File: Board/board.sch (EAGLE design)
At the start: 31 parts, among them IC1 MCP2300X/SO, IC2 LM1117, U1 ADS1015

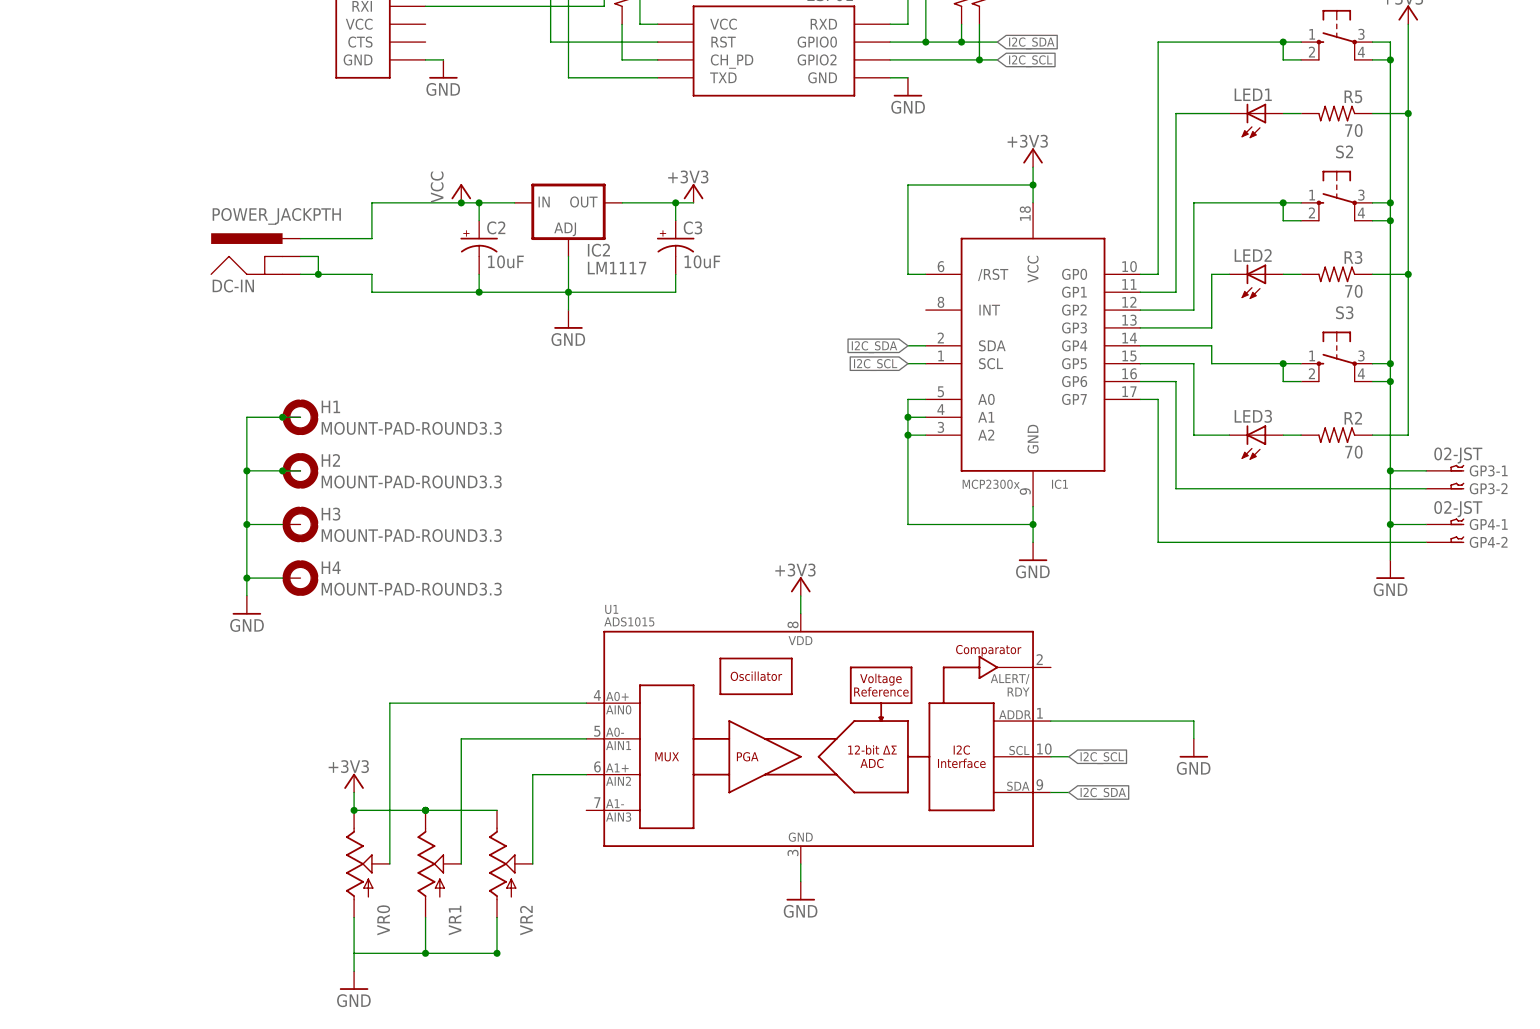
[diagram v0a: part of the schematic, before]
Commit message: Use cheaper ADC and add LEDs on spare GPIO
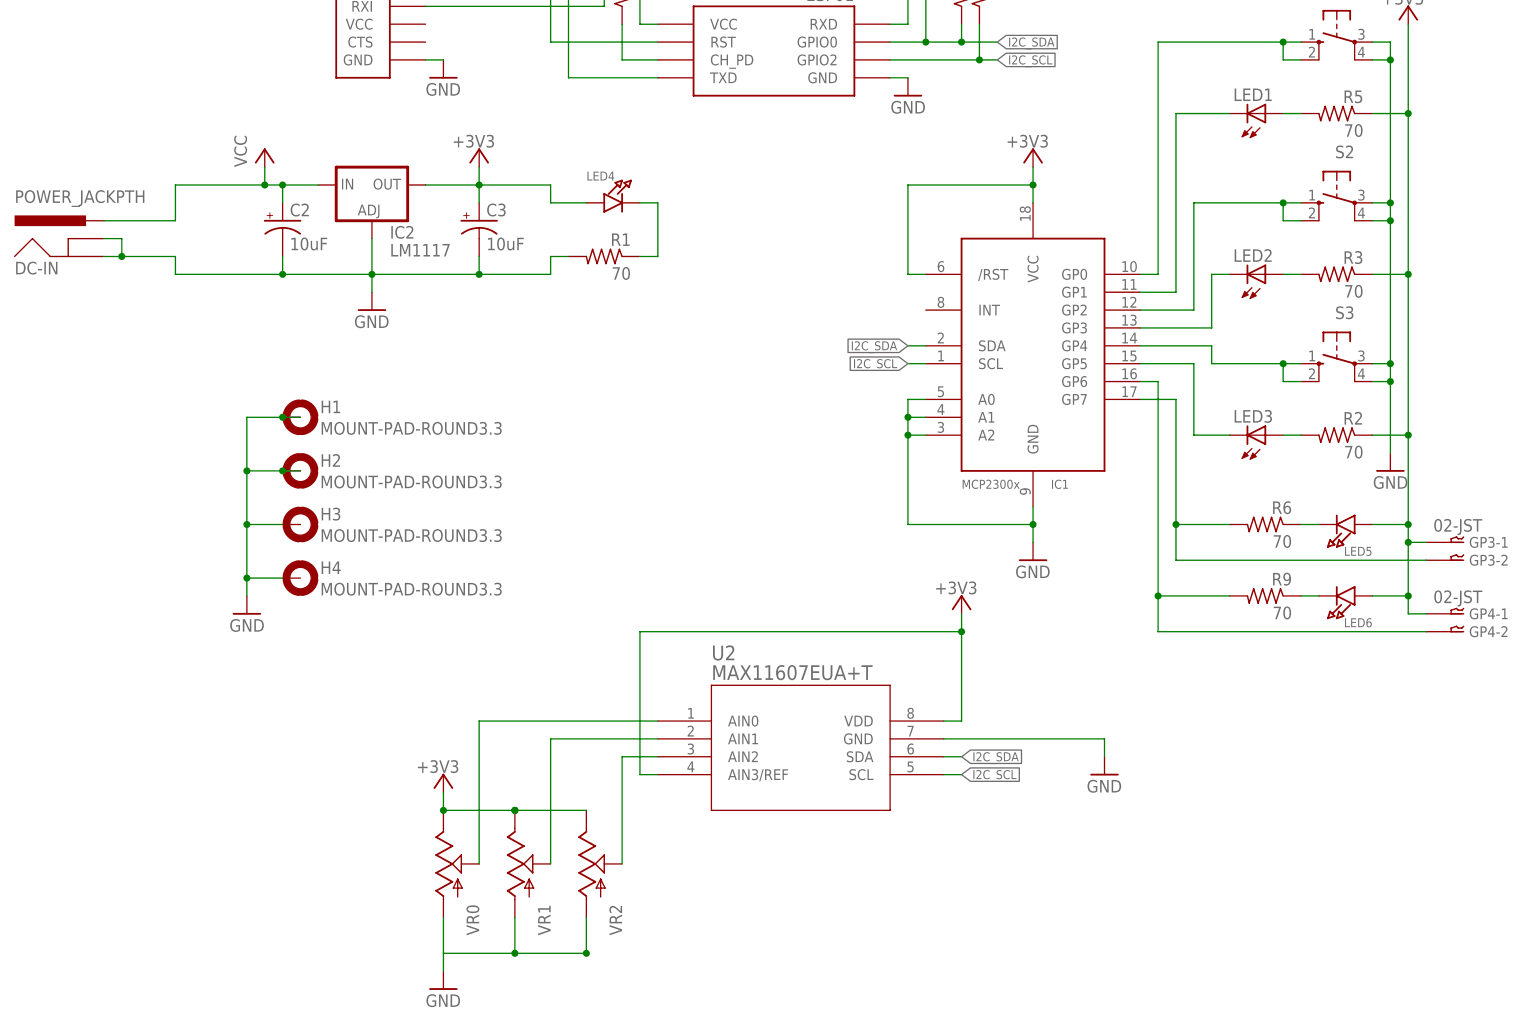
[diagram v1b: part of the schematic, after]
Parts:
- removed U1: ADS1015, SparkFun-AnalogIC:ADS1015
- added LED4, LED5, LED6: (no value), microbuilder:LED0805
- added R1, R6, R9: 70, resistor:R-US_R0603
- added U2: MAX11607EUA+T, MAX11607:MAX11607EUA+T
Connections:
- new net N$11: LED6.C, R9.1
- new net N$7: LED4.C, R1.1
- new net N$9: LED5.C, R6.1
- net +3V3: now also GP3-1.1, GP4-1.1, LED4.A, LED5.A, LED6.A, U2.AIN3/REF, U2.VDD; no longer U1.VDD
- net GND: now also R1.2, U2.GND; no longer GP3-1.1, GP4-1.1, U1.ADDR, U1.VSS
- net GP6: now also IC1.GP7, R6.2; no longer IC1.GP6
- net GP7: now also IC1.GP6, R9.2; no longer IC1.GP7
- net I2C_SCL: now also U2.SCL; no longer U1.SCL
- net I2C_SDA: now also U2.SDA; no longer U1.SDA
- net N$3: now also U2.AIN2; no longer U1.AIN2
- net N$4: now also U2.AIN1; no longer U1.AIN1
- net N$5: now also U2.AIN0; no longer U1.AIN0
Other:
- moved on the sheet: C2, C3, DC-IN, GP3-1, GP3-2, GP4-1, GP4-2, IC2, VR0, VR1, VR2

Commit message: Finish routing PCB
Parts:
- removed D4: (no value), diode:DIODE-DO214AC
- removed DC-IN: POWER_JACKPTH, SparkFun-Connectors:POWER_JACKPTH
- removed ESP-01: ESP01, esp8266modules-pk:ESP01
- removed GP3, GP4: 02-JST, con-jst-xh:02-JST
- removed IC1: MCP2300X/SO, adafruit:MCP2300X/SO
- removed JP2: FTDI_DEVICE, SparkFun-Connectors:FTDI_DEVICE
- removed LED5, LED6: (no value), microbuilder:LED0805
- removed U2: MAX11607EUA+T, MAX11607:MAX11607EUA+T
- added C1: 47pF, rcl:C-USC0603
- added C5: 10nF, rcl:C-USC0603
- added D1, D2, D3: (no value), diode:DIODE-DO214AC
- added L1: (no value), SparkFun-Passives:INDUCTOR0805
- added T1, T2: (no value), transistor:MMBT918LT1-NPN-SOT23-BEC
- added U1: FTS31XS-U, SparkFun-DigitalIC:FT231XS
- added USB: USB-RECEPTABLE, daspilker:USB-RECEPTABLE
- added X1: (no value), adafruit:ESP-12
- C4: value .1uF -> 47pF; device SparkFun-Passives:CAP0603-CAP -> rcl:C-USC0603
- R6: value 70 -> 27
- R7: value 10k -> 27
- R8: value 10k -> 12k
- R9: value 70 -> 12k
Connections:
- removed net GP0: IC1.GP0, S1.S, S1.S1
- removed net GP1: IC1.GP1, LED1.C
- removed net GP2: IC1.GP2, S2.S, S2.S1
- removed net GP3: IC1.GP3, LED2.C
- removed net GP4: IC1.GP4, S3.S, S3.S1
- removed net GP5: IC1.GP5, LED3.C
- removed net GP6: GP3-2.1, IC1.GP7, R6.2
- removed net GP7: GP4-2.1, IC1.GP6, R9.2
- removed net I2C_SCL: ESP-01.GPIO2, IC1.SCL, R8.1, U2.SCL
- removed net I2C_SDA: D4.A, ESP-01.GPIO0, IC1.SDA, R7.1, U2.SDA
- removed net VCC: C2.+, DC-IN.PWR, IC2.IN
- new net ADC: D1.C, D2.C, D3.C, X1.ADC
- new net GPIO0: S2.S, S2.S1, T2.C, X1.GPIO0
- new net GPIO12: LED1.C, X1.GPIO12
- new net GPIO13: S1.S, S1.S1, X1.GPIO13
- new net GPIO14: LED2.C, X1.GPIO14
- new net GPIO15: VR2.E, X1.GPIO15
- new net GPIO16: LED3.C, X1.GPIO16
- new net GPIO2: S3.S, S3.S1, X1.GPIO2
- new net GPIO4: VR0.E, X1.GPIO4
- new net GPIO5: VR1.E, X1.GPIO5
- new net N$12: D3.A, VR2.S
- new net N$13: C1.2, R6.1, USB.D-
- new net N$14: R8.1, T2.E, U1.!DTR
- new net N$15: R9.1, T1.E, U1.!RTS
- new net N$16: R8.2, T1.B
- new net N$17: R9.2, T2.B
- new net N$19: U1.!RESET, U1.3V3OUT, U1.VCCIO
- new net N$20: C2.+, IC2.IN, L1.1, U1.VCC
- net +3V3: now also R1.1, X1.VCC; no longer ESP-01.VCC, GP3-1.1, GP4-1.1, IC1./RST, IC1.VCC, LED4.A, LED5.A, LED6.A, R7.2, R8.2, U2.AIN3/REF, U2.VDD, VR0.E, VR1.E, VR2.E
- net GND: now also C1.1, C4.1, C5.1, LED4.C, U1.GND@16, U1.GND@6, USB.GND, X1.GND; no longer DC-IN.GND, DC-IN.GNDBREAK, ESP-01.GND, IC1.A0, IC1.A1, IC1.A2, IC1.GND, JP2.GND, R1.2, U2.GND
- net N$1: now also X1.CH_PD; no longer ESP-01.CH_PD
- net N$11: now also D2.A, VR1.S; no longer LED6.C, R9.1
- net N$2: now also R7.1, USB.D+; no longer D4.C, JP2.DTR
- net N$3: now also R7.2, U1.USBDP; no longer U2.AIN2, VR2.S
- net N$4: now also LED4.A, R1.2; no longer U2.AIN1, VR1.S
- net N$5: now also D1.A; no longer U2.AIN0
- net N$7: now also C5.2, L1.2, USB.VCC; no longer LED4.C, R1.1
- net N$9: now also R6.2, U1.USBDM; no longer LED5.C, R6.1
- net RST: now also T1.C, X1.RESET; no longer C4.1, ESP-01.RST
- net RXI: now also U1.TXD, X1.RXD; no longer ESP-01.RXD, JP2.RXI
- net TXO: now also U1.RXD, X1.TXD; no longer ESP-01.TXD, JP2.TXO
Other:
- moved on the sheet: C2, C3, C4, H1, H2, H3, H4, IC2, LED4, R1, R6, R9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
